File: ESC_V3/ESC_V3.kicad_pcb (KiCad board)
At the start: 2 copper layers, 52 x 31 mm, 29 parts, among them J1 Conn_01x08_Male, J2 Conn_01x01_Male, J3 Conn_01x02_Male, J4 Conn_01x01_Male, J5 Conn_01x01_Male, Q1 MOSFET-NCH-2N7002PW, Q2 MOSFET-NCH-2N7002PW, Q3 MOSFET-NCH-2N7002PW, Q4 MOSFET-NCH-2N7002PW, Q5 MOSFET-NCH-2N7002PW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

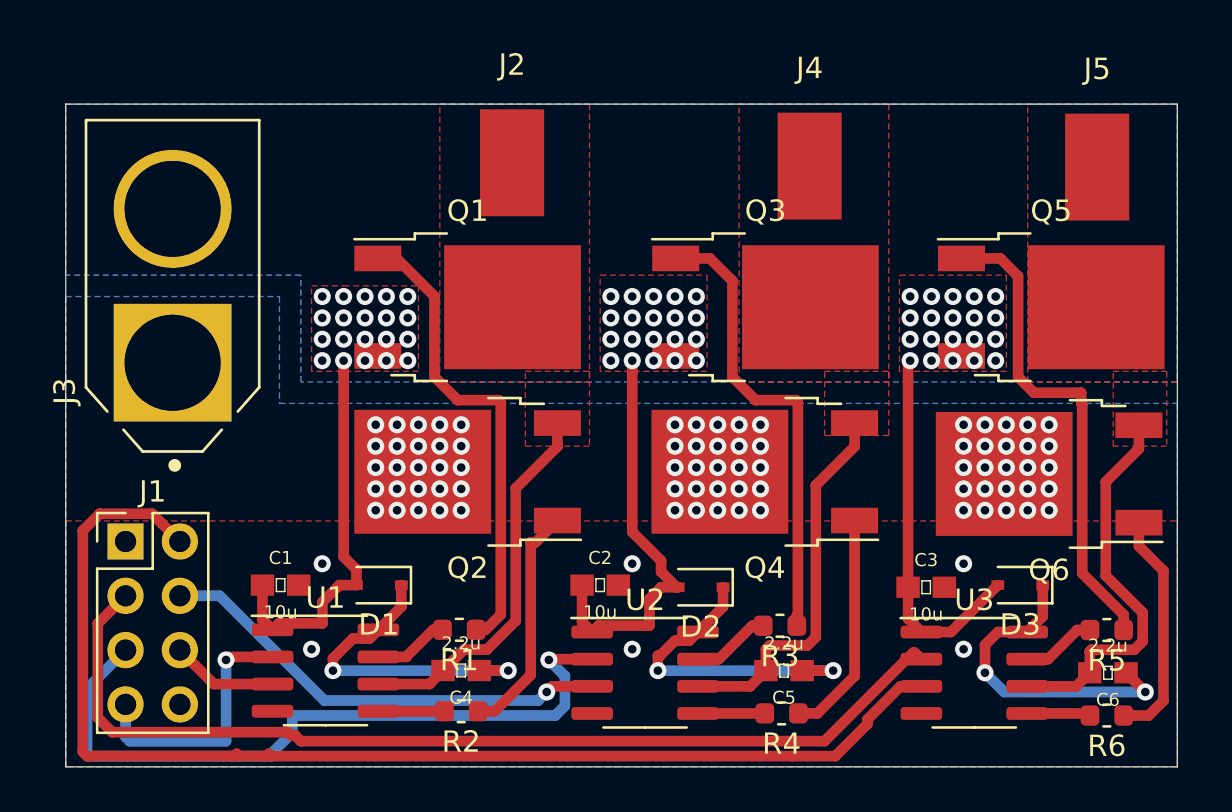
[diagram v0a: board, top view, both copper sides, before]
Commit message: Remap input pins to not be terrible
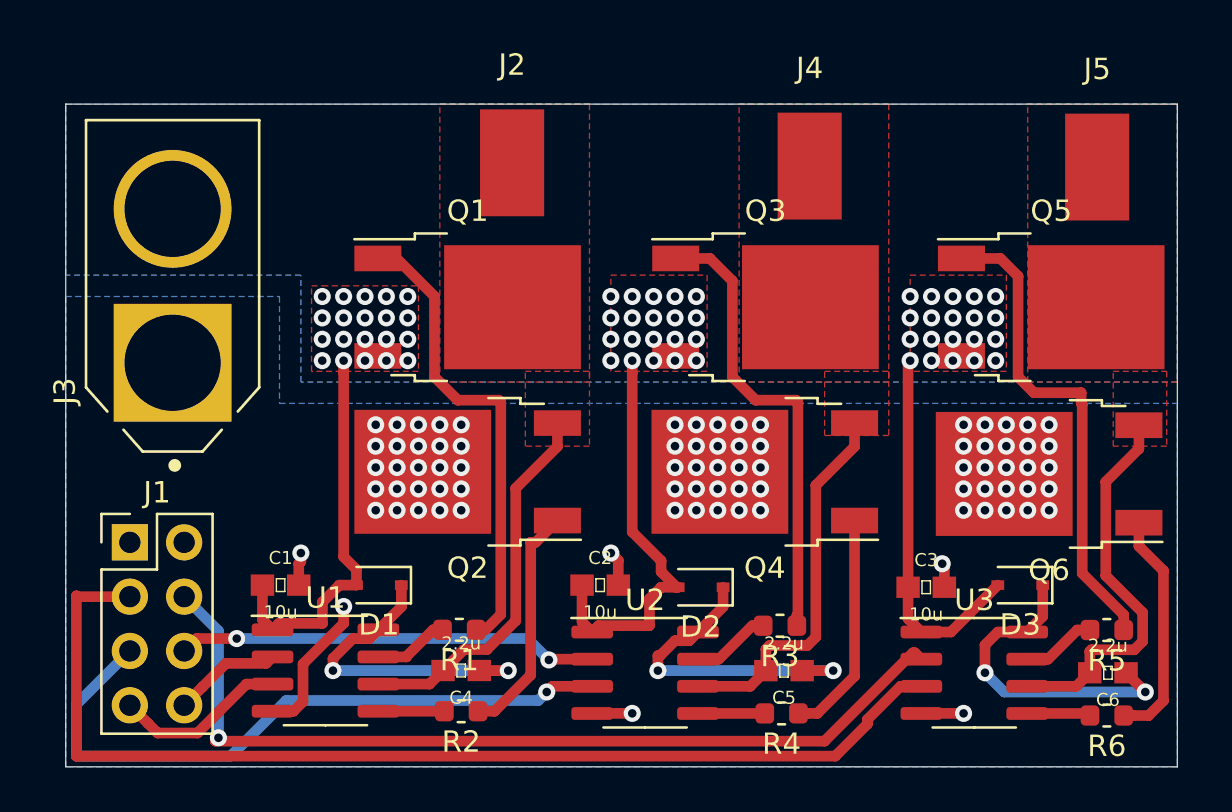
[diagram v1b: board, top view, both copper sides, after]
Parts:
- moved J1 0.20 mm to (107.0, 85.5)
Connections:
- J1 pad 2: L3 -> GND
- J1 pad 3: H3 -> L3
- J1 pad 4: L2 -> H3
- J1 pad 5: H2 -> L2
- J1 pad 6: L1 -> H2
- J1 pad 7: H1 -> L1
- J1 pad 8: GND -> H1
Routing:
- net GND: track 0.00 -> 15.0 mm
- net H2: track 34.0 -> 19.8 mm, vias 1 -> 2
- net L2: track 21.6 -> 31.4 mm
- net H1: track 12.3 -> 5.07 mm, vias 1 -> 0
- net L3: track 57.0 -> 51.0 mm
- net H3: track 47.1 -> 42.3 mm, vias 0 -> 1
- net L1: track 4.99 -> 8.16 mm
- removed copper zone on F.Cu, net GND

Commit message: minor cleanup
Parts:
- removed J2, J4, J5: Conn_01x01_Male, custom_library:3 solder pad
- added OUT 1: Conn_01x01_Male, custom_library:3 solder pad, F.Cu at (125.0, 67.8)
- added OUT 2: Conn_01x01_Male, custom_library:3 solder pad, F.Cu at (138.8, 67.8)
- added OUT 3: Conn_01x01_Male, custom_library:3 solder pad, F.Cu at (152.2, 67.8)
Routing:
- net L3: track 51.0 -> 48.3 mm
- net Net-(Q1-Pad1): track 22.1 -> 23.9 mm
- net L2: track 31.4 -> 30.3 mm
- net H3: track 42.3 -> 41.5 mm
- net Net-(Q3-Pad1): track 21.6 -> 22.2 mm
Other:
- board text added: "G"
- board text added: "H1"
- board text added: "H2"
- board text added: "H3"
- board text added: "L1"
- board text added: "L2"
- board text added: "L3"
